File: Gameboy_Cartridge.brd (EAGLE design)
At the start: 49.3 x 48 mm, 10 parts, among them IC1 AT49F040J

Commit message: Add VDD pour
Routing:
- net VDD: track 90.2 -> 0.00 mm
- net GND: track 119.1 -> 110.8 mm
- net 30: track 75.3 -> 74.2 mm
- added copper zone on layer 1, net VDD
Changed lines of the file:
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@@
 <contactref element="SJ1" pad="2"/>
 <contactref element="SJ3" pad="2"/>
-<wire x1="24.5053125" y1="44.7786" x2="24.1053125" y2="44.3786" width="0.1524" layer="1"/>
-<wire x1="24.1053125" y1="44.3786" x2="22.2053125" y2="44.3786" width="0.1524" layer="1"/>
-<wire x1="22.2053125" y1="44.3786" x2="17.95" y2="40.1232875" width="0.1524" layer="1"/>
-<wire x1="17.95" y1="40.1232875" x2="17.95" y2="38.74" width="0.1524" layer="1"/>
+<wire x1="17.95" y1="38.74" x2="17.95" y2="40.1232875" width="0.1524" layer="1"/>
 <wire x1="12.662" y1="35.8" x2="12.662" y2="37.2" width="0.1524" layer="1"/>
 <wire x1="12.662" y1="37.2" x2="14.162" y2="38.7" width="0.1524" layer="1"/>
@@
 <wire x1="36.9" y1="11.1" x2="48.7" y2="11.1" width="0.1524" layer="16"/>
 <via x="48.7" y="11.1" extent="1-16" drill="0.35"/>
-<wire x1="48.7" y1="11.1" x2="48.7" y2="5.5" width="0.1524" layer="1"/>
-<wire x1="48.7" y1="5.5" x2="49" y2="5.2" width="0.1524" layer="1"/>
-<wire x1="49" y1="3.6" x2="48.7" y2="3.3" width="0.1524" layer="1"/>
-<wire x1="48.7" y1="3.3" x2="48.8" y2="3.4" width="0.1524" layer="1"/>
-<wire x1="48.8" y1="3.4" x2="49" y2="3.4" width="0.1524" layer="1"/>
-<wire x1="24.55" y1="45" x2="24.55" y2="44.8232875" width="0.1524" layer="1"/>
-<wire x1="24.55" y1="44.8232875" x2="24.5053125" y2="44.7786" width="0.1524" layer="1"/>
 <wire x1="48.7" y1="11.1" x2="48.7" y2="45.7" width="0.1524" layer="1"/>
 <wire x1="48.7" y1="45.7" x2="48.6" y2="45.8" width="0.1524" layer="1"/>
-<wire x1="48.6" y1="45.8" x2="29.3" y2="45.8" width="0.1524" layer="1"/>
-<wire x1="29.3" y1="45.8" x2="28.8" y2="45.3" width="0.1524" layer="1"/>
-<via x="28.8" y="45.3" extent="1-16" drill="0.35"/>
-<wire x1="28.8" y1="45.3" x2="19.8" y2="45.3" width="0.1524" layer="16"/>
-<wire x1="19.8" y1="45.3" x2="19.7" y2="45.2" width="0.1524" layer="16"/>
-<via x="19.7" y="45.2" extent="1-16" drill="0.35"/>
-<wire x1="19.7" y1="45.2" x2="24.5" y2="45.2" width="0.1524" layer="1"/>
-<wire x1="24.75" y1="44.8" x2="24.55" y2="45" width="0.1524" layer="1"/>
-<wire x1="48.95" y1="4" x2="48.95" y2="3.65" width="0.1524" layer="1"/>
-<wire x1="48.95" y1="3.65" x2="49" y2="3.6" width="0.1524" layer="1"/>
+<wire x1="48.6" y1="45.8" x2="39.5" y2="45.8" width="0.1524" layer="1"/>
+<wire x1="39.5" y1="45.8" x2="39" y2="45.3" width="0.1524" layer="1"/>
+<via x="39" y="45.3" extent="1-16" drill="0.35"/>
 <wire x1="12.662" y1="35.8" x2="12.662" y2="34.4" width="0.1524" layer="1"/>
-<wire x1="49" y1="5.2" x2="48.95" y2="4" width="0" layer="19" extent="1-1"/>
-<wire x1="24.55" y1="45" x2="24.5" y2="45.2" width="0" layer="19" extent="1-1"/>
+<wire x1="23" y1="45.1732875" x2="23" y2="45.2" width="0.1524" layer="1"/>
+<via x="23" y="45.2" extent="1-16" drill="0.35"/>
+<wire x1="39" y1="45.3" x2="38.9" y2="45.2" width="0.1524" layer="16"/>
+<wire x1="38.9" y1="45.2" x2="23" y2="45.2" width="0.1524" layer="16"/>
+<wire x1="23" y1="45.2" x2="24.35" y2="45.2" width="0.1524" layer="1"/>
+<wire x1="24.35" y1="45.2" x2="24.55" y2="45" width="0.1524" layer="1"/>
+<wire x1="17.95" y1="40.1232875" x2="23" y2="45.1732875" width="0.1524" layer="1"/>
+<wire x1="48.95" y1="4" x2="48.7" y2="4.25" width="0.1524" layer="1"/>
+<wire x1="48.7" y1="4.25" x2="48.7" y2="11.1" width="0.1524" layer="1"/>
 </signal>
 <signal name="VDD">
@@
 <contactref element="R1" pad="2"/>
 <contactref element="C1" pad="1"/>
-<wire x1="31.7" y1="43" x2="36.7" y2="43" width="0.1524" layer="1"/>
-<wire x1="36.7" y1="43" x2="38.12" y2="41.58" width="0.1524" layer="1"/>
-<wire x1="38.12" y1="41.58" x2="39.03" y2="41.58" width="0.1524" layer="1"/>
-<wire x1="2.05" y1="4" x2="2.05" y2="19.65" width="0.1524" layer="1"/>
-<wire x1="2.05" y1="19.65" x2="6.35" y2="23.95" width="0.1524" layer="1"/>
-<wire x1="2.05" y1="19.65" x2="2.05" y2="36.95" width="0.1524" layer="1"/>
-<wire x1="2.05" y1="36.95" x2="12.5" y2="47.4" width="0.1524" layer="1"/>
-<wire x1="12.5" y1="47.4" x2="26.9" y2="47.4" width="0.1524" layer="1"/>
-<wire x1="26.45" y1="45" x2="26.9" y2="45.45" width="0.1524" layer="1"/>
-<wire x1="26.9" y1="45.45" x2="26.9" y2="47.4" width="0.1524" layer="1"/>
-<wire x1="26.55" y1="44.9" x2="26.45" y2="45" width="0.1524" layer="1"/>
-<wire x1="26.55" y1="43.45" x2="26.55" y2="44.9" width="0.1524" layer="1"/>
-<wire x1="39.37" y1="37.2" x2="39.37" y2="41.24" width="0.1524" layer="1"/>
-<wire x1="39.37" y1="41.24" x2="39.03" y2="41.58" width="0.1524" layer="1"/>
-<wire x1="27" y1="43" x2="26.55" y2="43.45" width="0.1524" layer="1"/>
-<wire x1="31.7" y1="43" x2="27" y2="43" width="0.1524" layer="1"/>
+<polygon width="0.1524" layer="1">
+<vertex x="2.8" y="7"/>
+<vertex x="2.8" y="18.9"/>
+<vertex x="7.3" y="23.4"/>
+<vertex x="7.3" y="24.54"/>
+<vertex x="5.16" y="24.54"/>
+<vertex x="3" y="26.7"/>
+<vertex x="3" y="37.6"/>
+<vertex x="11.8" y="46.4"/>
+<vertex x="25.9" y="46.4"/>
+<vertex x="25.9" y="42.9"/>
+<vertex x="26.1" y="42.7"/>
+<vertex x="35.7" y="42.7"/>
+<vertex x="39.1" y="39.3"/>
+<vertex x="39.1" y="38"/>
+<vertex x="39.2" y="37.9"/>
+<vertex x="39.7" y="37.9"/>
+<vertex x="39.7" y="43.4"/>
+<vertex x="35.2" y="47.9"/>
+<vertex x="0.9" y="47.9"/>
+<vertex x="0.9" y="7.5"/>
+<vertex x="1.4" y="7"/>
+</polygon>
 </signal>
 <signal name="6">
@@
 <contactref element="U$2" pad="16"/>
 <contactref element="SJ3" pad="1"/>
-<wire x1="6.38" y1="34.6" x2="6.35" y2="34.57" width="0.1524" layer="1"/>
 <wire x1="15.3" y1="33.7" x2="9.8" y2="33.7" width="0.1524" layer="1"/>
 <wire x1="15.3" y1="33.7" x2="15.3" y2="37.9" width="0.1524" layer="1"/>
 <via x="15.3" y="37.9" extent="1-16" drill="0.35"/>
-<wire x1="15.3" y1="37.9" x2="16.7" y2="39.3" width="0.1524" layer="16"/>
+<wire x1="15.3" y1="37.9" x2="16.6" y2="39.2" width="0.1524" layer="16"/>
 <via x="36.8" y="39.3" extent="1-16" drill="0.35"/>
-<wire x1="16.7" y1="39.3" x2="25.2302" y2="39.3" width="0.1524" layer="16"/>
-<wire x1="36.8" y1="39.3" x2="25.2302" y2="39.3" width="0.1524" layer="16"/>
+<wire x1="16.6" y1="39.2" x2="25.2302" y2="39.2" width="0.1524" layer="16"/>
+<wire x1="36.8" y1="39.3" x2="36.7" y2="39.2" width="0.1524" layer="16"/>
+<wire x1="36.7" y1="39.2" x2="25.2302" y2="39.2" width="0.1524" layer="16"/>
 <wire x1="36.8" y1="39.3" x2="36.8" y2="37.23" width="0.1524" layer="1"/>
 <wire x1="36.8" y1="37.23" x2="36.83" y2="37.2" width="0.1524" layer="1"/>
@@
 <contactref element="U$2" pad="10"/>
 <contactref element="U$1" pad="30"/>
-<wire x1="45.75" y1="4" x2="45.95" y2="4.2" width="0.1524" layer="1"/>
 <wire x1="17.95" y1="35.86" x2="21.56" y2="35.86" width="0.1524" layer="1"/>
 <via x="34.9" y="42.1" extent="1-16" drill="0.35"/>
@@
 <wire x1="47.5" y1="19" x2="45.8" y2="17.3" width="0.1524" layer="16"/>
 <via x="45.8" y="17.3" extent="1-16" drill="0.35"/>
-<wire x1="45.8" y1="17.3" x2="45.8" y2="5.5" width="0.1524" layer="1"/>
-<wire x1="45.8" y1="5.5" x2="45.9" y2="5.4" width="0.1524" layer="1"/>
-<wire x1="45.9" y1="5.4" x2="45.9" y2="3.2" width="0.1524" layer="1"/>
 <wire x1="45.4" y1="43.4" x2="47.5" y2="41.3" width="0.1524" layer="16"/>
 <wire x1="21.56" y1="35.86" x2="23" y2="37.3" width="0.1524" layer="1"/>
@@
 <wire x1="34.8698" y1="42.1302" x2="34.9" y2="42.1" width="0.1524" layer="1"/>
 <wire x1="34.8698" y1="42.1302" x2="23.3302" y2="42.1302" width="0.1524" layer="1"/>
-<wire x1="45.9" y1="3.2" x2="45.75" y2="4" width="0" layer="19" extent="1-1"/>
+<wire x1="45.75" y1="4" x2="45.75" y2="17.25" width="0.1524" layer="1"/>
+<wire x1="45.75" y1="17.25" x2="45.8" y2="17.3" width="0.1524" layer="1"/>
 </signal>
 <signal name="4">
@@
 <wire x1="41.91" y1="35.71" x2="41.91" y2="37.2" width="0.1524" layer="1"/>
 <via x="39.9" y="44.7" extent="1-16" drill="0.35"/>
-<wire x1="39.9" y1="44.7" x2="39.9" y2="42.4832875" width="0.1524" layer="1"/>
-<wire x1="39.9" y1="42.4832875" x2="39.9086" y2="42.4746875" width="0.1524" layer="1"/>
-<wire x1="39.9086" y1="42.4746875" x2="39.9086" y2="40.6853125" width="0.1524" layer="1"/>
-<wire x1="39.9086" y1="40.6853125" x2="39.9" y2="40.6767125" width="0.1524" layer="1"/>
-<wire x1="39.9" y1="40.6767125" x2="39.9" y2="35.7" width="0.1524" layer="1"/>
+<wire x1="39.9" y1="44.7" x2="39.9086" y2="44.6914" width="0.1524" layer="1"/>
+<wire x1="39.9086" y1="44.6914" x2="39.9086" y2="35.6914" width="0.1524" layer="1"/>
 <wire x1="40.4" y1="35.2" x2="41.4" y2="35.2" width="0.1524" layer="1"/>
-<wire x1="39.9" y1="35.7" x2="40.4" y2="35.2" width="0.1524" layer="1"/>
+<wire x1="39.9086" y1="35.6914" x2="40.4" y2="35.2" width="0.1524" layer="1"/>
 <wire x1="39.9" y1="44.7" x2="39.8952" y2="44.7048" width="0.1524" layer="16"/>
 <wire x1="39.8952" y1="44.7048" x2="38.07374375" y2="44.7048" width="0.1524" layer="16"/>
@@
 <via x="16.4" y="40.9" extent="1-16" drill="0.35"/>
 <wire x1="16.4" y1="40.9" x2="21.9" y2="40.9" width="0.1524" layer="16"/>
-<wire x1="28.1" y1="41.1" x2="37" y2="41.1" width="0.1524" layer="16"/>
-<wire x1="28.1" y1="41.1" x2="26.8" y2="42.4" width="0.1524" layer="16"/>
-<via x="37" y="41.1" extent="1-16" drill="0.35"/>
-<wire x1="37" y1="41.1" x2="38.1" y2="40" width="0.1524" layer="1"/>
-<wire x1="38.1" y1="40" x2="38.1" y2="37.2" width="0.1524" layer="1"/>
+<wire x1="28.2" y1="41" x2="36.3" y2="41" width="0.1524" layer="16"/>
+<wire x1="28.2" y1="41" x2="26.8" y2="42.4" width="0.1524" layer="16"/>
+<via x="36.3" y="41" extent="1-16" drill="0.35"/>
+<wire x1="36.3" y1="41" x2="36.5" y2="41" width="0.1524" layer="1"/>
+<wire x1="38.1" y1="39.4" x2="36.5" y2="41" width="0.1524" layer="1"/>
+<wire x1="38.1" y1="39.4" x2="38.1" y2="37.2" width="0.1524" layer="1"/>
 <wire x1="21.9" y1="40.9" x2="23.4" y2="42.4" width="0.1524" layer="16"/>
 <wire x1="23.4" y1="42.4" x2="26.8" y2="42.4" width="0.1524" layer="16"/>

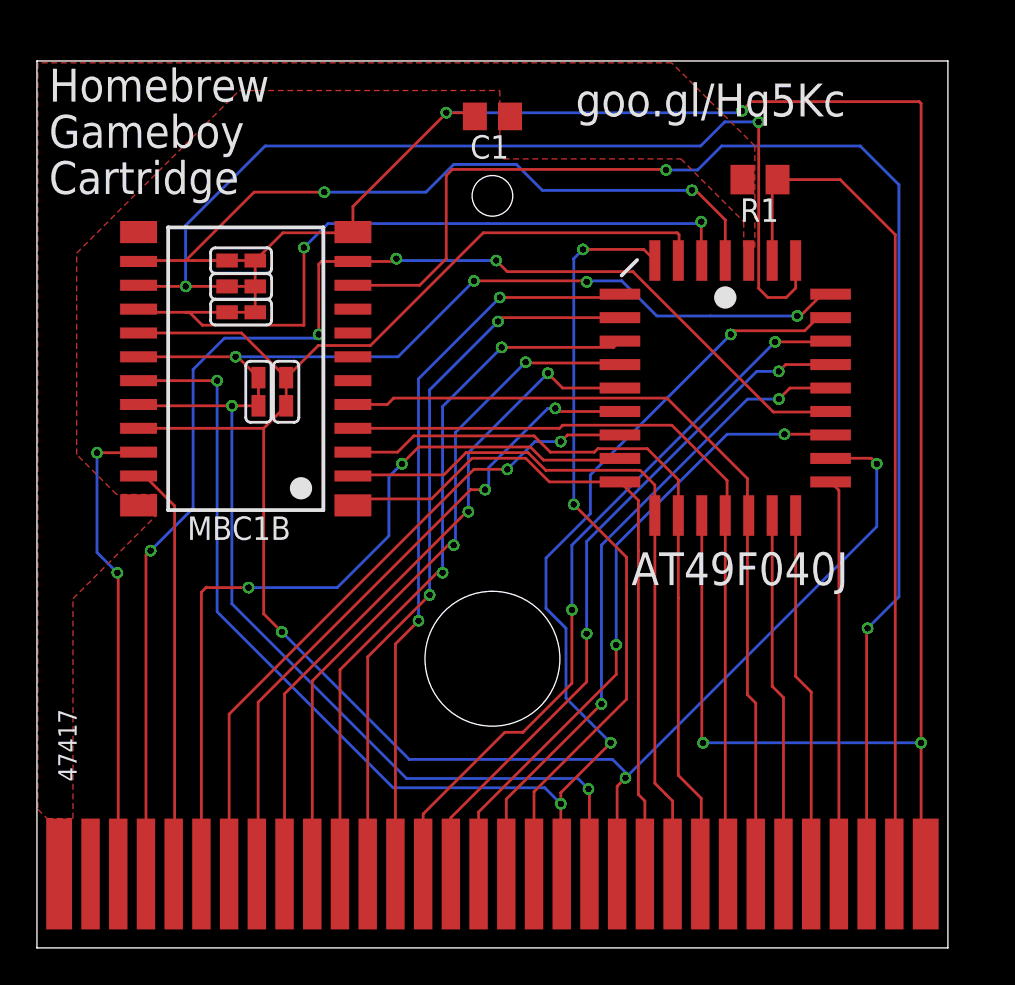
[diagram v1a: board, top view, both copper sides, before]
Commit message: Add GND pour
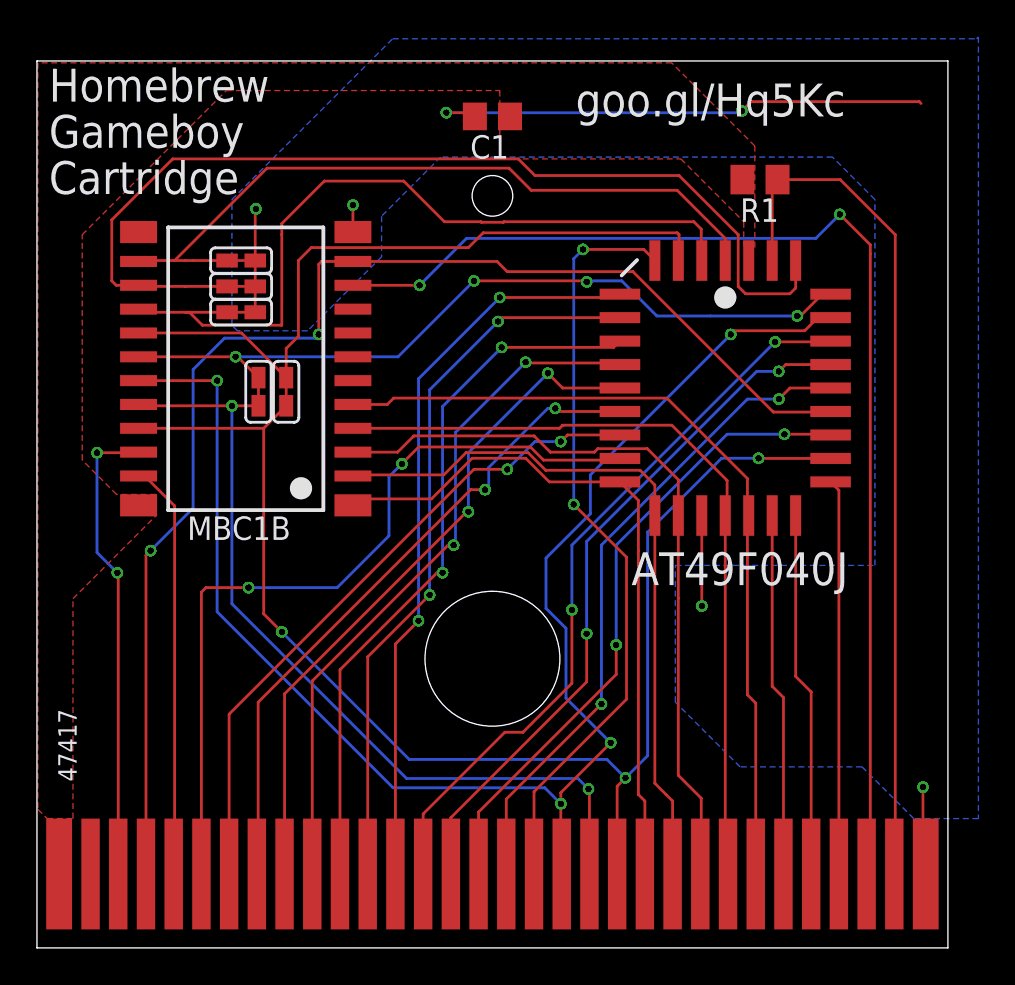
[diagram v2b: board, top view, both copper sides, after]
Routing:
- net GND: track 110.8 -> 44.7 mm, vias 4 -> 6
- net 30: track 74.2 -> 64.4 mm
- net D: track 36.0 -> 39.3 mm
- net C: track 39.9 -> 42.4 mm, vias 2 -> 0
- net 4: track 71.4 -> 71.2 mm, vias 4 -> 2
- net A: track 39.6 -> 39.5 mm, vias 2 -> 0
- net B: track 54.4 -> 54.3 mm, vias 2 -> 0
- added copper zone on layer 16, net GND

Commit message: Pretty happy with the routing now
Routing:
- net GND: track 44.7 -> 34.7 mm, vias 6 -> 5
- net E: track 42.2 -> 45.7 mm, vias 4 -> 2
- net 6: track 43.4 -> 41.1 mm, vias 2 -> 0
- net 19: track 81.4 -> 79.8 mm
- net 30: track 64.4 -> 63.2 mm
- net 7: track 36.1 -> 37.2 mm
- net 22: track 37.8 -> 36.8 mm
- net B: track 54.3 -> 55.2 mm
- net A: track 39.5 -> 40.2 mm
- net 18: track 41.4 -> 42.1 mm
- net C: track 42.4 -> 43.1 mm
- net 23: track 39.4 -> 38.8 mm
- net 24: track 41.0 -> 40.4 mm
